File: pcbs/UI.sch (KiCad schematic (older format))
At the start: 0 parts

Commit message: Almost done with schematics. SPI OLED is missing.
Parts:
- added C? (x4): 10n, Resistors_SMD:R_0603, symbol C
- added R? (x9): 10k, Resistors_SMD:R_0603, symbol R
- added SW?: SW_Push_Dual, MyTactileSW:SW_PUSH_TE_CONN_6x6, symbol SW_Push_Dual
- added SW? (x2): Rotary_Encoder, MyTactileSW:ROT_ENC_EN12_TT_Electronics_No_Switch, symbol Rotary_Encoder
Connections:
- new net: R?.2, R?.2, SW?.1 (A) (x2)
- new net: R?.2, R?.2, SW?.3 (B) (x2)
- new net 3V3: R?.1, R?.1, R?.1, R?.1, R?.1
- new net GND: C?.2, C?.2, C?.2, C?.2, SW?.2, SW?.2 (C), SW?.2 (C), SW?.4
- new net ROT_ENC_11: C?.1, C?.1, R?.1, R?.1
- new net ROT_ENC_12: C?.1, C?.1, R?.1, R?.1
- new net UI_BUTTON: R?.2, SW?.1, SW?.3

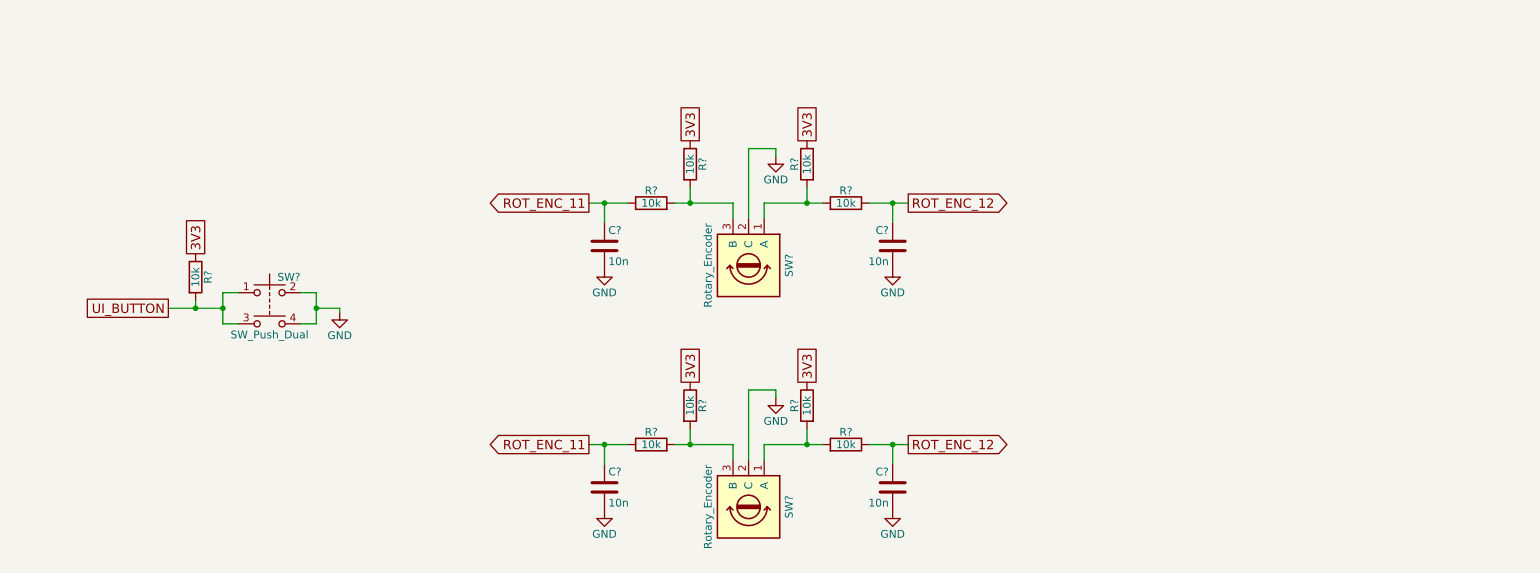
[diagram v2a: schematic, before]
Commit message: No DRC errors anymore in schematics.
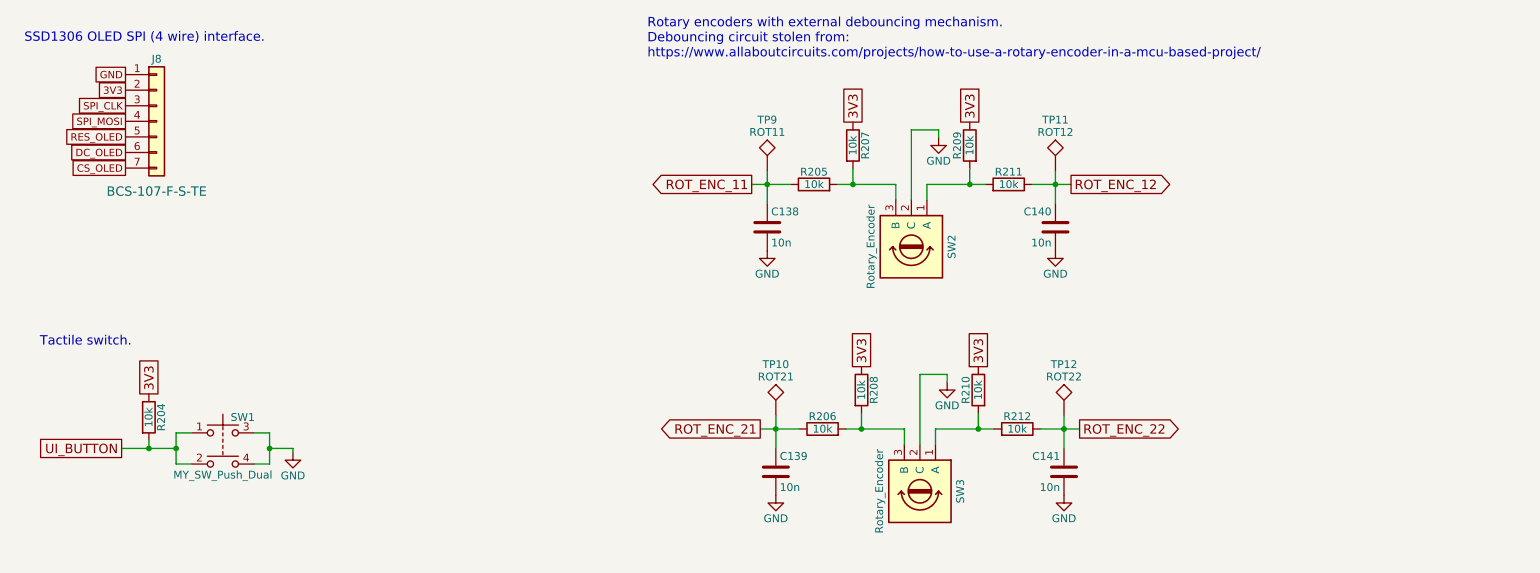
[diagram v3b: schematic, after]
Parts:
- removed C? (x2): 10n, Resistors_SMD:R_0603, symbol C
- removed R? (x4): 10k, Resistors_SMD:R_0603, symbol R
- removed SW?: SW_Push_Dual, MyTactileSW:SW_PUSH_TE_CONN_6x6, symbol SW_Push_Dual
- removed SW?: Rotary_Encoder, MyTactileSW:ROT_ENC_EN12_TT_Electronics_No_Switch, symbol Rotary_Encoder
- added C138, C140: 10n, Resistors_SMD:R_0603, symbol C
- added J8: Conn_01x07, Pin_Headers:Pin_Header_Straight_1x07_Pitch2.54mm, symbol Conn_01x07
- added R205, R207, R209, R211: 10k, Resistors_SMD:R_0603, symbol R
- added SW1: MY_SW_Push_Dual, MySWs:SW_PUSH_TE_CONN_6x6, symbol MY_SW_Push_Dual
- added SW2: Rotary_Encoder, MyTactileSW:ROT_ENC_EN12_TT_Electronics_No_Switch, symbol Rotary_Encoder
- added TP10: ROT21, symbol TEST
- added TP11: ROT12, symbol TEST
- added TP12: ROT22, symbol TEST
- added TP9: ROT11, symbol TEST
- gave numbers to parts that had none: 8
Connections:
- net 3V3: now also J8.2 (Pin_2), R207.1, R209.1
- net GND: now also C138.2, C140.2, J8.1 (Pin_1), SW1.3, SW1.4, SW2.2 (C)
- net ROT_ENC_11: now also C138.1, R205.1, TP9.1; no longer C139.1, R206.1
- net ROT_ENC_12: now also C140.1, R211.1, TP11.1; no longer C141.1, R212.1
- net UI_BUTTON: now also SW1.1, SW1.2
- new net: R209.2, R211.2, SW2.1 (A)
- new net: R205.2, R207.2, SW2.3 (B)
- new net CS_OLED: J8.7 (Pin_7)
- new net DC_OLED: J8.6 (Pin_6)
- new net RES_OLED: J8.5 (Pin_5)
- new net ROT_ENC_21: C139.1, R206.1, TP10.1
- new net ROT_ENC_22: C141.1, R212.1, TP12.1
- new net SPI_CLK: J8.3 (Pin_3)
- new net SPI_MOSI: J8.4 (Pin_4)
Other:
- note added: "Rotary encoders with external debouncing mechanism. \nDebouncing circuit stolen from:\nhttps://www.allaboutcircuits.com/projects/how-to-use-a-rotary-encoder-in-a-mcu-based-project/"
- note added: "SSD1306 OLED SPI (4 wire) interface."
- note added: "Tactile switch."
- moved on the sheet: C139, C141, R204, R206, R208, R210, R212, SW3
